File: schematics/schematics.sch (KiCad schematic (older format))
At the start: 13 parts, among them J1 Screw_Terminal_01x02, J2 Screw_Terminal_01x02, J3 Screw_Terminal_01x02, J4 Screw_Terminal_01x02, J5 Screw_Terminal_01x02

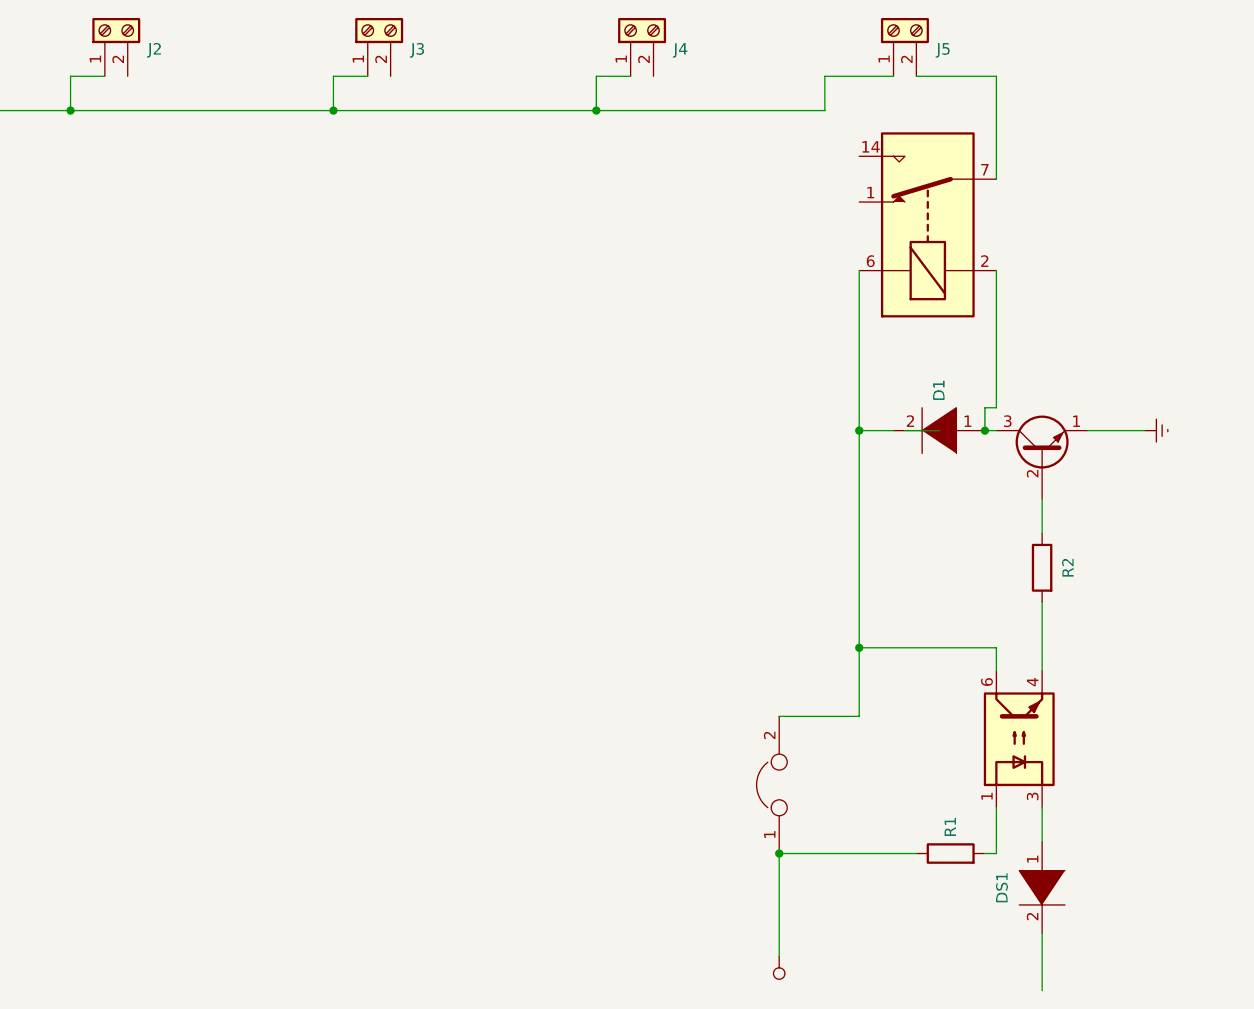
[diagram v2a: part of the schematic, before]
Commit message: Add second and third circuits for the pumps
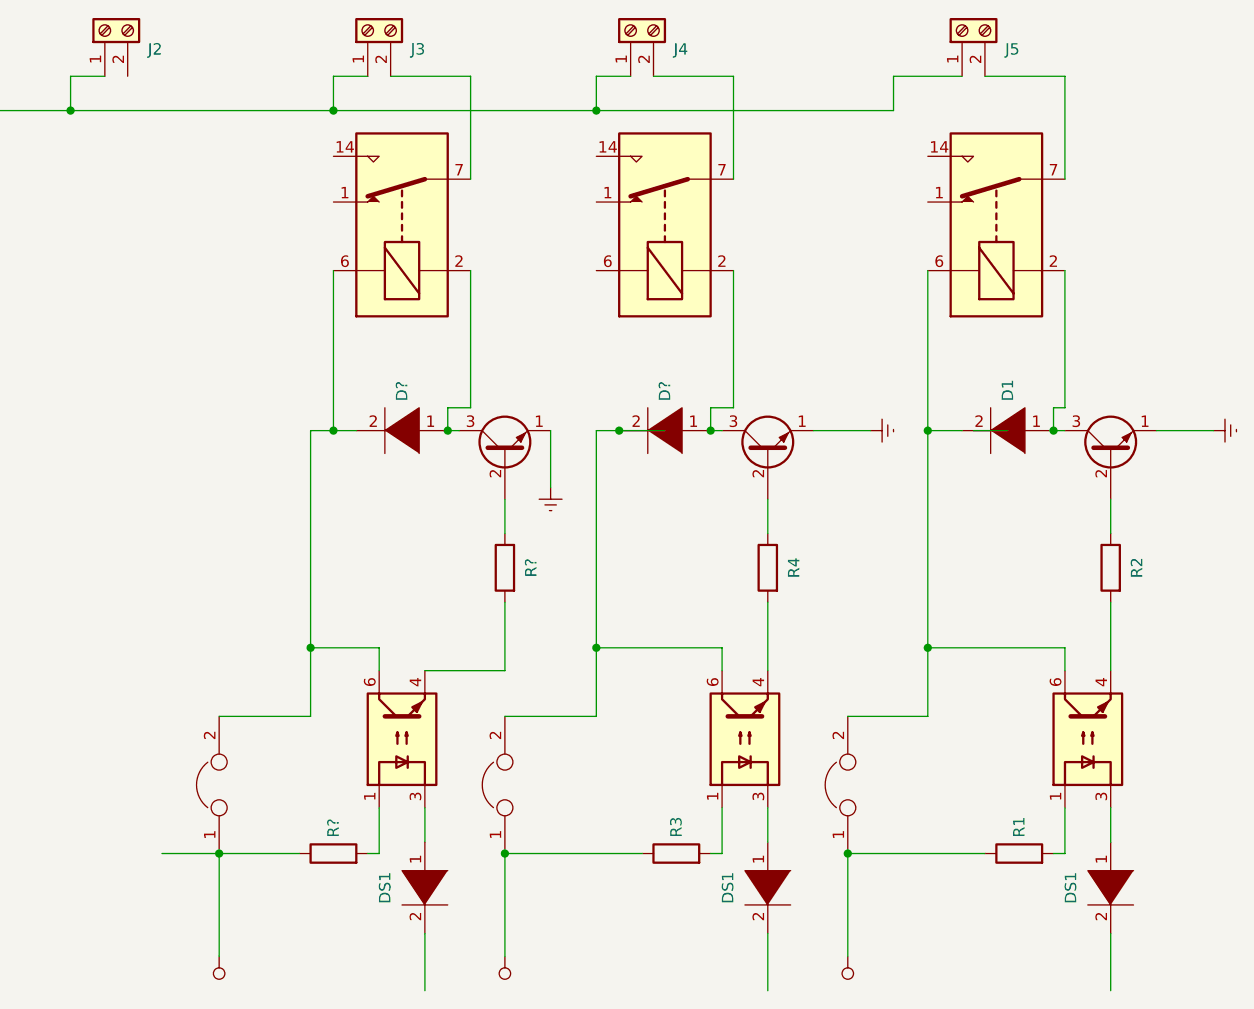
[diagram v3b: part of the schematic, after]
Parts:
- added D? (x2): DIODE, symbol pspice:DIODE
- added D? (x2): DS1, symbol pspice:DIODE
- added JP? (x2): Jumper, symbol Device:Jumper
- added K? (x2): DIPxx-1Cxx-51x, Relay_THT:Relay_StandexMeder_DIP_LowProfile, symbol Relay:DIPxx-1Cxx-51x
- added Q? (x2): 2N2219, Package_TO_SOT_THT:TO-39-3, symbol Transistor_BJT:2N2219
- added R3, R4, R? (x2): R, symbol Device:R
- added U? (x2): TLP185, Package_SO:SOIC-4_4.55x3.7mm_P2.54mm, symbol Isolator:TLP185
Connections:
- wire segments 36 -> 83
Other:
- moved on the sheet: D1, J5, R1, R2

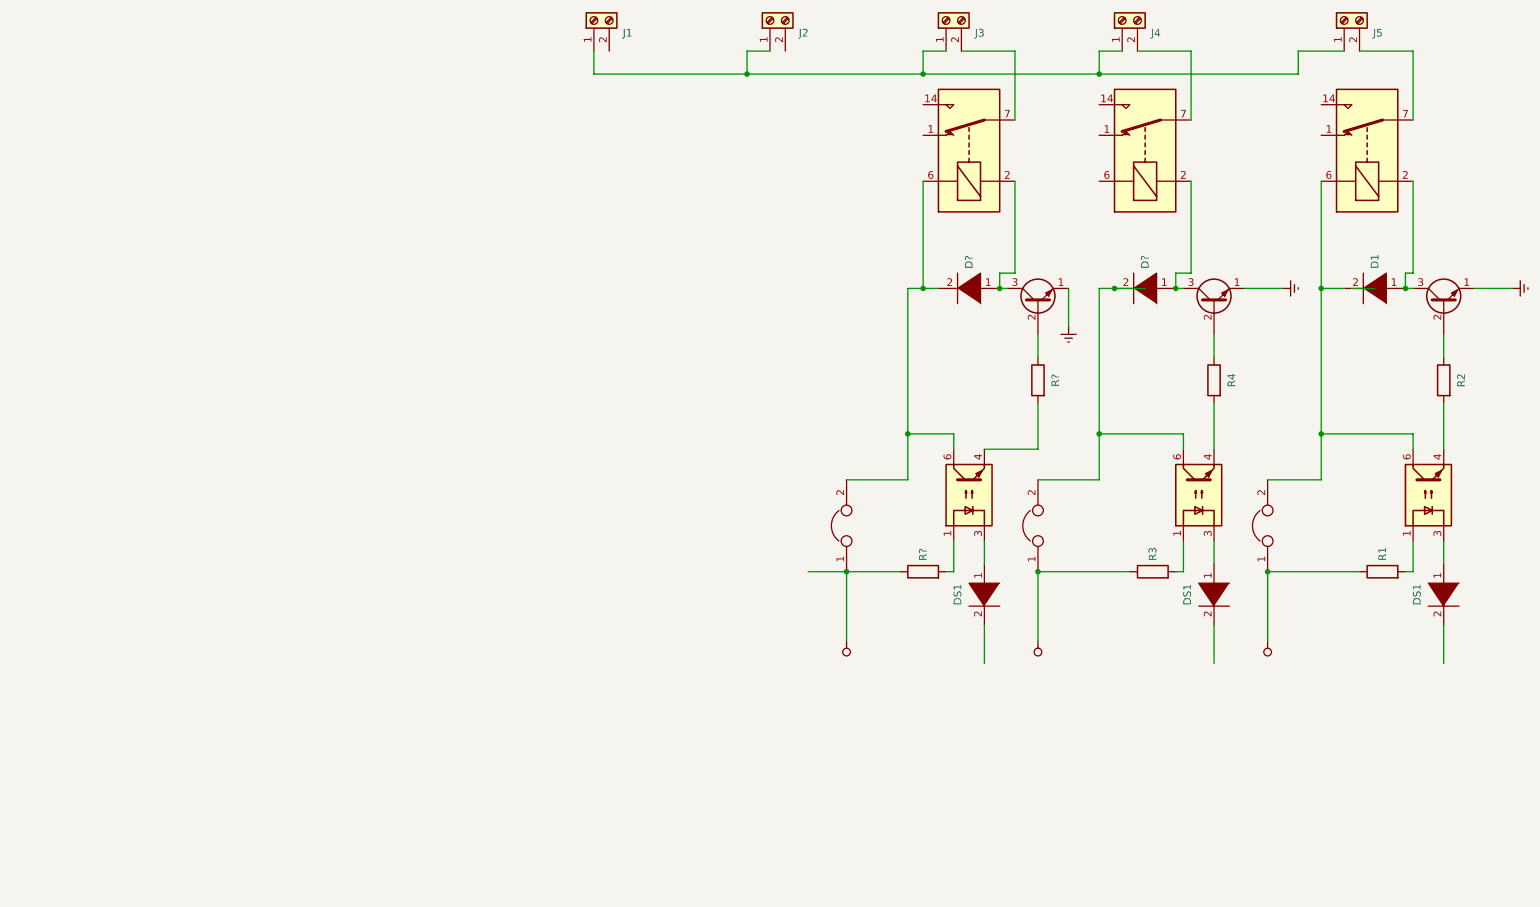
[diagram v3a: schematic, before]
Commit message: Add last two circuits for the pumps
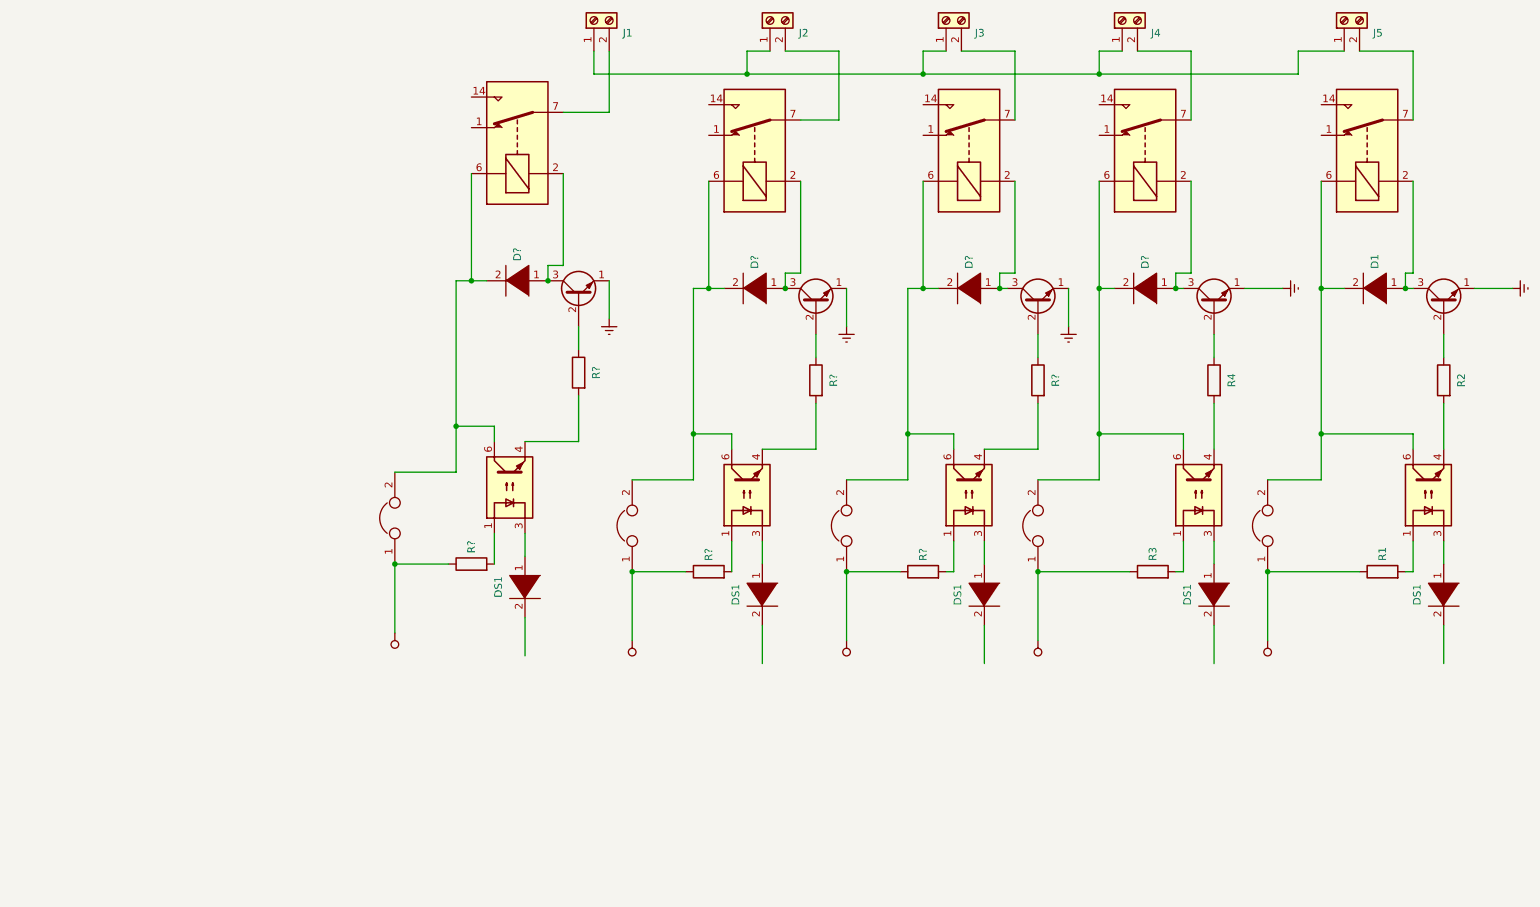
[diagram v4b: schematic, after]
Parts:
- added D? (x2): DIODE, symbol pspice:DIODE
- added D? (x2): DS1, symbol pspice:DIODE
- added JP? (x2): Jumper, symbol Device:Jumper
- added K? (x2): DIPxx-1Cxx-51x, Relay_THT:Relay_StandexMeder_DIP_LowProfile, symbol Relay:DIPxx-1Cxx-51x
- added Q? (x2): 2N2219, Package_TO_SOT_THT:TO-39-3, symbol Transistor_BJT:2N2219
- added R? (x4): R, symbol Device:R
- added U? (x2): TLP185, Package_SO:SOIC-4_4.55x3.7mm_P2.54mm, symbol Isolator:TLP185
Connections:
- wire segments 83 -> 126

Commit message: Rename the elements
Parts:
- removed D?: DIODE, symbol pspice:DIODE
- removed D?: DS1, symbol pspice:DIODE
- removed JP?: Jumper, symbol Device:Jumper
- removed K?: DIPxx-1Cxx-51x, Relay_THT:Relay_StandexMeder_DIP_LowProfile, symbol Relay:DIPxx-1Cxx-51x
- removed Q?: 2N2219, Package_TO_SOT_THT:TO-39-3, symbol Transistor_BJT:2N2219
- removed R? (x2): R, symbol Device:R
- removed U?: TLP185, Package_SO:SOIC-4_4.55x3.7mm_P2.54mm, symbol Isolator:TLP185
- D?: value DS1 -> DS4
- D?: value DS1 -> DS3
- D?: value DS1 -> DS2
- gave numbers to parts that had none: 7
- renumbered D1 to D4, J1 to J1-220V, R3 to R5, R4 to R6, R1 to R7, R2 to R8
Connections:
- wire segments 126 -> 104
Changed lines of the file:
@@
 $EndDescr
 $Comp
-L Connector:Screw_Terminal_01x02 J1
+L Connector:Screw_Terminal_01x02 J1-220V
 U 1 1 5C8BD117
 P 5100 1300
-F 0 "J1" V 5018 1112 50  0000 R CNN
+F 0 "J1-220V" V 5018 1112 50  0000 R CNN
 F 1 "Screw_Terminal_01x02" V 4973 1112 50  0001 R CNN
 F 2 "" H 5100 1300 50  0001 C CNN
@@
 $EndComp
 $Comp
-L Device:R R1
+L Device:R R7
 U 1 1 5C8BA970
 P 10250 4900
-F 0 "R1" H 10320 4900 50  0000 L CNN
+F 0 "R7" H 10320 4900 50  0000 L CNN
 F 1 "R" H 10320 4855 50  0001 L CNN
 F 2 "" V 10180 4900 50  0001 C CNN
@@
 P 10650 5050
 F 0 "D?" H 10650 4785 50  0001 C CNN
-F 1 "DS1" H 10650 4876 50  0000 C CNN
+F 1 "DS4" H 10650 4876 50  0000 C CNN
 F 2 "" H 10650 5050 50  0001 C CNN
 F 3 "~" H 10650 5050 50  0001 C CNN
@@
 	10650 4100 10650 3800
 $Comp
-L Device:R R2
+L Device:R R8
 U 1 1 5C8C515D
 P 10650 3650
-F 0 "R2" V 10535 3650 50  0000 C CNN
+F 0 "R8" V 10535 3650 50  0000 C CNN
 F 1 "R" V 10534 3650 50  0001 C CNN
 F 2 "" V 10580 3650 50  0001 C CNN
@@
 	9000 2350 9000 2950
 $Comp
-L pspice:DIODE D?
+L pspice:DIODE D3
 U 1 1 5C9280CF
 P 8700 3050
-F 0 "D?" V 8700 2922 50  0000 R CNN
+F 0 "D3" V 8700 2922 50  0000 R CNN
 F 1 "DIODE" V 8655 2922 50  0001 R CNN
 F 2 "" H 8700 3050 50  0001 C CNN
@@
 	10450 2950 10400 2950
 $Comp
-L pspice:DIODE D1
+L pspice:DIODE D4
 U 1 1 5C8C3A6E
 P 10200 3050
-F 0 "D1" V 10200 2922 50  0000 R CNN
+F 0 "D4" V 10200 2922 50  0000 R CNN
 F 1 "DIODE" V 10155 2922 50  0001 R CNN
 F 2 "" H 10200 3050 50  0001 C CNN
@@
 	8900 2950 8900 3050
 $Comp
-L Device:R R3
+L Device:R R5
 U 1 1 5C942F30
 P 8750 4900
-F 0 "R3" H 8820 4900 50  0000 L CNN
+F 0 "R5" H 8820 4900 50  0000 L CNN
 F 1 "R" H 8820 4855 50  0001 L CNN
 F 2 "" V 8680 4900 50  0001 C CNN
@@
 P 9150 5050
 F 0 "D?" H 9150 4785 50  0001 C CNN
-F 1 "DS1" H 9150 4876 50  0000 C CNN
+F 1 "DS3" H 9150 4876 50  0000 C CNN
 F 2 "" H 9150 5050 50  0001 C CNN
 F 3 "~" H 9150 5050 50  0001 C CNN
@@
 	9150 4100 9150 3800
 $Comp
-L Device:R R4
+L Device:R R6
 U 1 1 5C942F53
 P 9150 3650
-F 0 "R4" V 9035 3650 50  0000 C CNN
+F 0 "R6" V 9035 3650 50  0000 C CNN
 F 1 "R" V 9034 3650 50  0001 C CNN
 F 2 "" V 9080 3650 50  0001 C CNN
@@
 	8000 4100 8000 3800
 $Comp
-L Device:R R?
+L Device:R R4
 U 1 1 5C969249
 P 8000 3650
-F 0 "R?" V 7885 3650 50  0000 C CNN
+F 0 "R4" V 7885 3650 50  0000 C CNN
 F 1 "R" V 7884 3650 50  0001 C CNN
 F 2 "" V 7930 3650 50  0001 C CNN
@@
 	8000 4100 7650 4100
 $Comp
-L Device:R R?
+L Device:R R3
 U 1 1 5C96C914
 P 7250 4900
-F 0 "R?" H 7320 4900 50  0000 L CNN
+F 0 "R3" H 7320 4900 50  0000 L CNN
 F 1 "R" H 7320 4855 50  0001 L CNN
 F 2 "" V 7180 4900 50  0001 C CNN
@@
 P 7650 5050
 F 0 "D?" H 7650 4785 50  0001 C CNN
-F 1 "DS1" H 7650 4876 50  0000 C CNN
+F 1 "DS2" H 7650 4876 50  0000 C CNN
 F 2 "" H 7650 5050 50  0001 C CNN
 F 3 "~" H 7650 5050 50  0001 C CNN
@@
 Connection ~ 7750 3050
 $Comp
-L pspice:DIODE D?
+L pspice:DIODE D2
 U 1 1 5C962393
 P 7550 3050
-F 0 "D?" V 7550 2922 50  0000 R CNN
+F 0 "D2" V 7550 2922 50  0000 R CNN
 F 1 "DIODE" V 7505 2922 50  0001 R CNN
 F 2 "" H 7550 3050 50  0001 C CNN
@@
 	6350 2950 6350 3050
 $Comp
-L pspice:DIODE D?
+L pspice:DIODE D1
 U 1 1 5C9B4E98
 P 6150 3050
-F 0 "D?" V 6150 2922 50  0000 R CNN
+F 0 "D1" V 6150 2922 50  0000 R CNN
 F 1 "DIODE" V 6105 2922 50  0001 R CNN
 F 2 "" H 6150 3050 50  0001 C CNN
@@
 	6550 4100 6550 3800
 $Comp
-L Device:R R?
+L Device:R R2
 U 1 1 5C9D96AF
 P 6550 3650
-F 0 "R?" V 6435 3650 50  0000 C CNN
+F 0 "R2" V 6435 3650 50  0000 C CNN
 F 1 "R" V 6434 3650 50  0001 C CNN
 F 2 "" V 6480 3650 50  0001 C CNN
@@
 $EndComp
 $Comp
-L Device:R R?
+L Device:R R1
 U 1 1 5C9F5EFC
 P 5850 4900
-F 0 "R?" H 5920 4900 50  0000 L CNN
+F 0 "R1" H 5920 4900 50  0000 L CNN
 F 1 "R" H 5920 4855 50  0001 L CNN
 F 2 "" V 5780 4900 50  0001 C CNN
@@
 $EndComp
 Connection ~ 5350 4900
-Wire Wire Line
-	5200 1500 5200 1900
-$Comp
-L Relay:DIPxx-1Cxx-51x K?
-U 1 1 5CA0E1FC
-P 4600 2100
-F 0 "K?" H 5030 2146 50  0001 L CNN
-F 1 "DIPxx-1Cxx-51x" H 5030 2100 50  0001 L CNN
-F 2 "Relay_THT:Relay_StandexMeder_DIP_LowProfile" H 5050 2050 50  0001 L CNN
-F 3 "https://standexelectronics.com/wp-content/uploads/datasheet_reed_relay_DIP.pdf" H 4600 2100 50  0001 C CNN
-	1    4600 2100
-	0    -1   -1   0
-$EndComp
-Wire Wire Line
-	4300 2300 4300 3000
-Wire Wire Line
-	4300 3000 4400 3000
-Wire Wire Line
-	4200 3950 4200 3000
-Wire Wire Line
-	4300 3000 4200 3000
-Connection ~ 4300 3000
-$Comp
-L pspice:DIODE D?
-U 1 1 5CA17594
-P 4600 3000
-F 0 "D?" V 4600 2872 50  0000 R CNN
-F 1 "DIODE" V 4555 2872 50  0001 R CNN
-F 2 "" H 4600 3000 50  0001 C CNN
-F 3 "~" H 4600 3000 50  0001 C CNN
-	1    4600 3000
-	-1   0    0    1
-$EndComp
-Wire Wire Line
-	4900 2300 4900 2900
-Wire Wire Line
-	4800 3000 4800 2900
-Wire Wire Line
-	4800 2900 4900 2900
-$Comp
-L Transistor_BJT:2N2219 Q?
-U 1 1 5CA29775
-P 5000 3100
-F 0 "Q?" H 5190 3146 50  0001 L CNN
-F 1 "2N2219" H 5190 3100 50  0001 L CNN
-F 2 "Package_TO_SOT_THT:TO-39-3" H 5200 3025 50  0001 L CIN
-F 3 "http://www.onsemi.com/pub_link/Collateral/2N2219-D.PDF" H 5000 3100 50  0001 L CNN
-	1    5000 3100
-	0    -1   -1   0
-$EndComp
-$Comp
-L power:GNDREF #PWR?
-U 1 1 5CA2977F
-P 5200 3250
-F 0 "#PWR?" H 5200 3000 50  0001 C CNN
-F 1 "GNDREF" H 5205 3077 50  0001 C CNN
-F 2 "" H 5200 3250 50  0001 C CNN
-F 3 "" H 5200 3250 50  0001 C CNN
-	1    5200 3250
-	1    0    0    -1
-$EndComp
-Wire Wire Line
-	5200 3000 5200 3250
-Wire Wire Line
-	5000 3450 5000 3300
-Connection ~ 4800 3000
-Wire Wire Line
-	5000 4050 5000 3750
-$Comp
-L Device:R R?
-U 1 1 5CA2F6CA
-P 5000 3600
-F 0 "R?" V 4885 3600 50  0000 C CNN
-F 1 "R" V 4884 3600 50  0001 C CNN
-F 2 "" V 4930 3600 50  0001 C CNN
-F 3 "~" H 5000 3600 50  0001 C CNN
-	1    5000 3600
-	-1   0    0    -1
-$EndComp
-Wire Wire Line
-	5000 4050 4650 4050
-$Comp
-L Isolator:TLP185 U?
-U 1 1 5CA351A6
-P 4550 4350
-F 0 "U?" H 4550 4675 50  0001 C CNN
-F 1 "TLP185" H 4550 4583 50  0001 C CNN
-F 2 "Package_SO:SOIC-4_4.55x3.7mm_P2.54mm" H 4550 4050 50  0001 C CIN
-F 3 "https://toshiba.semicon-storage.com/info/docget.jsp?did=11791&prodName=TLP185" H 4550 4350 50  0001 L CNN
-	1    4550 4350
-	0    -1   -1   0
-$EndComp
-Wire Wire Line
-	4450 4050 4450 3950
-Wire Wire Line
-	4200 3950 4450 3950
-Wire Wire Line
-	3800 4250 4200 4250
-Wire Wire Line
-	4200 4250 4200 3950
-Connection ~ 4200 3950
-$Comp
-L Device:Jumper JP?
-U 1 1 5CA40696
-P 3800 4550
-F 0 "JP?" H 3800 4814 50  0001 C CNN
-F 1 "Jumper" H 3800 4723 50  0001 C CNN
-F 2 "" H 3800 4550 50  0001 C CNN
-F 3 "~" H 3800 4550 50  0001 C CNN
-	1    3800 4550
-	0    -1   -1   0
-$EndComp
-$Comp
-L Device:R R?
-U 1 1 5CA45F48
-P 4300 4850
-F 0 "R?" H 4370 4850 50  0000 L CNN
-F 1 "R" H 4370 4805 50  0001 L CNN
-F 2 "" V 4230 4850 50  0001 C CNN
-F 3 "~" H 4300 4850 50  0001 C CNN
-	1    4300 4850
-	0    -1   -1   0
-$EndComp
-Wire Wire Line
-	3800 4850 4150 4850
-Wire Wire Line
-	4450 4850 4450 4650
-Wire Wire Line
-	4650 4650 4650 4800
-$Comp
-L pspice:DIODE D?
-U 1 1 5CA45F55
-P 4650 5000
-F 0 "D?" H 4650 4735 50  0001 C CNN
-F 1 "DS1" H 4650 4826 50  0000 C CNN
-F 2 "" H 4650 5000 50  0001 C CNN
-F 3 "~" H 4650 5000 50  0001 C CNN
-	1    4650 5000
-	0    1    1    0
-$EndComp
-Wire Wire Line
-	4650 5200 4650 5450
-Wire Wire Line
-	3800 4850 3800 5300
-$Comp
-L power:VCC #PWR?
-U 1 1 5CA4C7CC
-P 3800 5300
-F 0 "#PWR?" H 3800 5150 50  0001 C CNN
-F 1 "VCC" V 3818 5427 50  0001 L CNN
-F 2 "" H 3800 5300 50  0001 C CNN
-F 3 "" H 3800 5300 50  0001 C CNN
-	1    3800 5300
-	-1   0    0    1
-$EndComp
-Connection ~ 3800 4850
-Wire Wire Line
-	4900 1900 5200 1900
 $EndSCHEMATC
